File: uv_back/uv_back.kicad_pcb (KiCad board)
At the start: 2 copper layers, 75 x 174.2 mm, 0 parts

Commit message: setting up for KiCad v6.01
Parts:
- added U1: OPA1656ID, Package_SO:SOIC-8_3.9x4.9mm_P1.27mm, B.Cu at (67.6, 102.2)
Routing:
- net (no net): vias 4 -> 0
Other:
- board size 75 x 174.2 mm -> 74.8 x 173.9 mm

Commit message: dev update
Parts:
- added C1: 0.1uF, Resistor_SMD:R_0603_1608Metric, F.Cu at (99.8, 148.2)
- added C2: 0.1uF, Resistor_SMD:R_0603_1608Metric, F.Cu at (108.3, 134.2)
- added C3: 10000pF, Capacitor_SMD:C_0603_1608Metric, F.Cu at (87.4, 158.8)
- added C4: 1uF, Capacitor_SMD:C_0805_2012Metric, F.Cu at (87.6, 153.6)
- added C5: 10000pF, Capacitor_SMD:C_0603_1608Metric, F.Cu at (91.8, 153.3)
- added J1: B2B-PH-SM4-TB(LF)(SN), Connector_JST:JST_PH_B2B-PH-SM4-TB_1x02-1MP_P2.00mm_Vertical, F.Cu at (92.6, 138.2)
- added J2: B3B-PH-SM4-TB(LF)(SN), Connector_JST:JST_PH_B3B-PH-SM4-TB_1x03-1MP_P2.00mm_Vertical, F.Cu at (62.2, 120.3)
- added J3: B2B-PH-SM4-TB(LF)(SN), Connector_JST:JST_PH_B2B-PH-SM4-TB_1x02-1MP_P2.00mm_Vertical, F.Cu at (92.6, 147.8)
- added J4: B3B-PH-SM4-TB(LF)(SN), Connector_JST:JST_PH_B3B-PH-SM4-TB_1x03-1MP_P2.00mm_Vertical, F.Cu at (81.2, 138.2)
- added J5: B3B-PH-SM4-TB(LF)(SN), Connector_JST:JST_PH_B3B-PH-SM4-TB_1x03-1MP_P2.00mm_Vertical, F.Cu at (81.2, 147.8)
- added J6: B3B-PH-SM4-TB(LF)(SN), Connector_JST:JST_PH_B3B-PH-SM4-TB_1x03-1MP_P2.00mm_Vertical, F.Cu at (68.7, 157.3)
- added J7: B2B-PH-SM4-TB(LF)(SN), Connector_JST:JST_PH_B2B-PH-SM4-TB_1x02-1MP_P2.00mm_Vertical, F.Cu at (80.2, 157.3)
- added J8: B3B-PH-SM4-TB(LF)(SN), Connector_JST:JST_PH_B3B-PH-SM4-TB_1x03-1MP_P2.00mm_Vertical, F.Cu at (68.7, 147.8)
- added R1: 10k, Resistor_SMD:R_0603_1608Metric, F.Cu at (99.8, 145.7)
- added R10: 2k, Resistor_SMD:R_0603_1608Metric, F.Cu at (95.9, 153.3)
- added R11: 50, Resistor_SMD:R_0603_1608Metric, F.Cu at (103.9, 143.2)
- added R2: 10k, Resistor_SMD:R_0603_1608Metric, F.Cu at (112.3, 134.2)
- added R3: 0, Resistor_SMD:R_0603_1608Metric, F.Cu at (108.3, 136.7)
- added R4: 0, Resistor_SMD:R_0603_1608Metric, F.Cu at (87.4, 156.3)
- added R5: 1k, Resistor_SMD:R_0603_1608Metric, F.Cu at (99.8, 140.7)
- added R6: 2k, Resistor_SMD:R_0603_1608Metric, F.Cu at (91.4, 156.3)
- added R7: 1k, Resistor_SMD:R_0603_1608Metric, F.Cu at (103.9, 140.7)
- added R8: 2k, Resistor_SMD:R_0603_1608Metric, F.Cu at (108.3, 139.2)
- added R9: 2k, Resistor_SMD:R_0603_1608Metric, F.Cu at (99.8, 143.2)
- added U2: OPA1656ID, Package_SO:SOIC-8_3.9x4.9mm_P1.27mm, F.Cu at (102.1, 136.2)
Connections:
- U1 pad 1: unconnected-(U1-Pad1) -> Net-(C3-Pad2)
- U1 pad 2: unconnected-(U1-Pad2) -> Net-(C3-Pad1)
- U1 pad 3: unconnected-(U1-Pad3) -> /VMID
- U1 pad 4: unconnected-(U1-Pad4) -> GND
- U1 pad 5: unconnected-(U1-Pad5) -> Net-(J2-Pad2)
- U1 pad 6: unconnected-(U1-Pad6) -> Net-(R3-Pad1)
- U1 pad 7: unconnected-(U1-Pad7) -> Net-(R3-Pad1)
- U1 pad 8: unconnected-(U1-Pad8) -> +9V

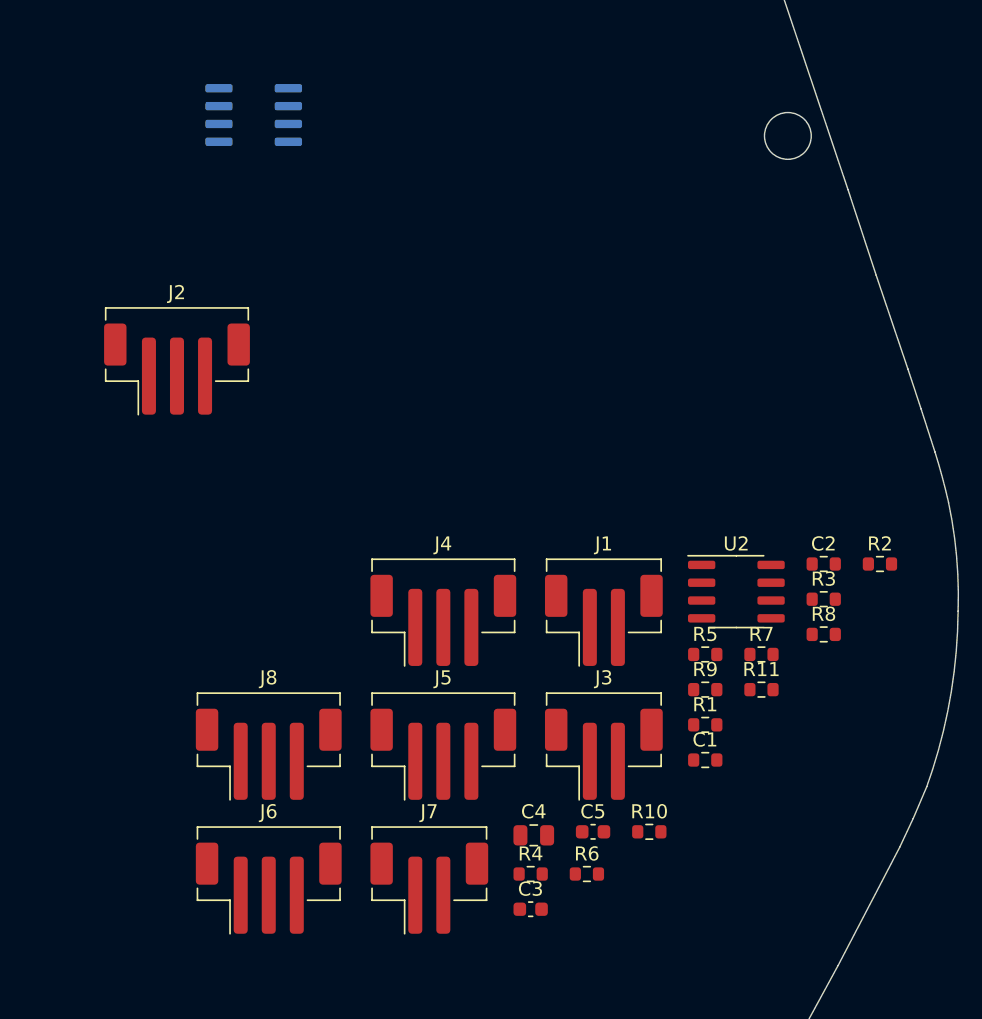
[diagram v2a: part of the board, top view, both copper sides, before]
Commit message: connector and 3d model updates
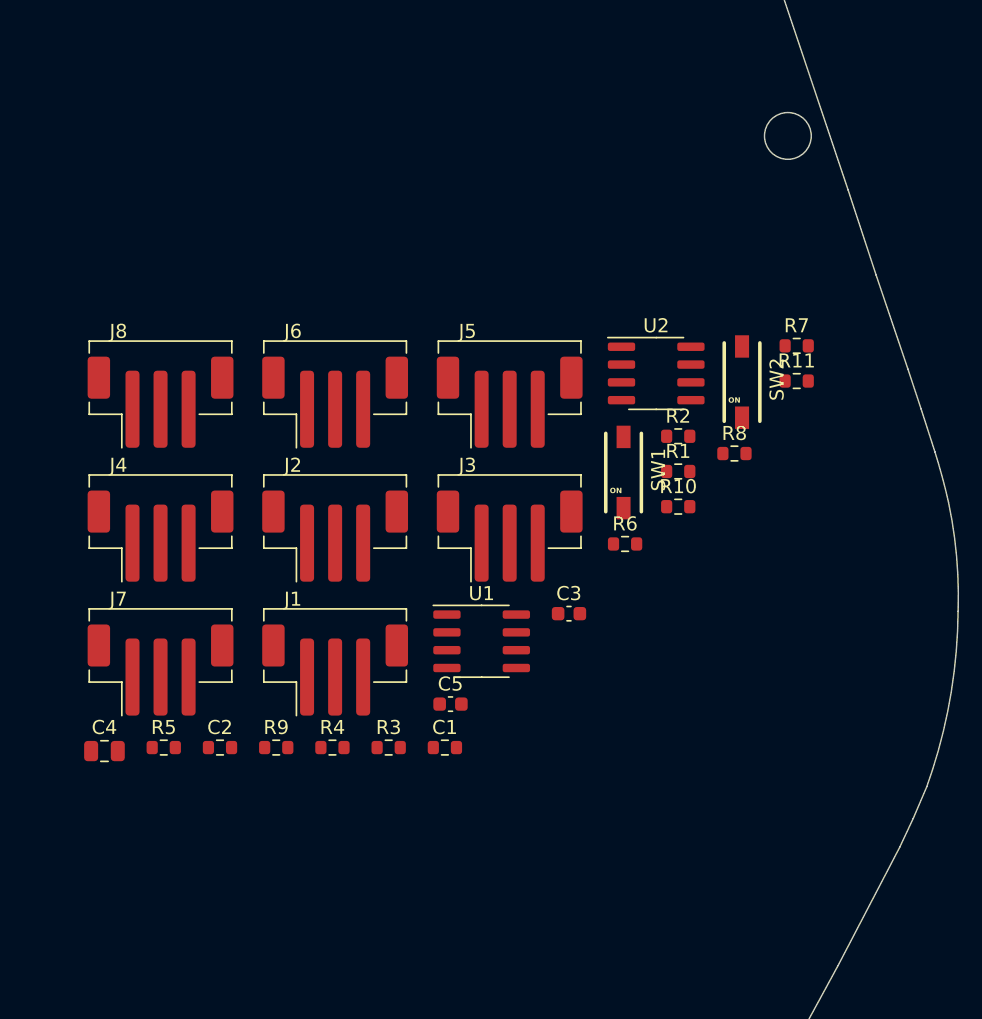
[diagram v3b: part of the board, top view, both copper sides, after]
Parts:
- added SW1: CHS01TA, eElectroMechanical:CHS-01TA, F.Cu at (94.0, 127.7)
- added SW2: CHS01TA, eElectroMechanical:CHS-01TA, F.Cu at (102.5, 121.3)
- J1, J3, J7: value B2B-PH-SM4-TB(LF)(SN) -> B3B-PH-SM4-TBT(LF)(SN); footprint Connector_JST:JST_PH_B2B-PH-SM4-TB_1x02-1MP_P2.00mm_Vertical -> eConnector_JST_PSH:B3B-PH-SM4
- J2, J4, J8: value B3B-PH-SM4-TB(LF)(SN) -> B3B-PH-SM4-TBT(LF)(SN); footprint Connector_JST:JST_PH_B3B-PH-SM4-TB_1x03-1MP_P2.00mm_Vertical -> eConnector_JST_PSH:B3B-PH-SM4
- J5, J6: value B3B-PH-SM4-TB(LF)(SN) -> B3B-PH-SM4-TBT(LF)(SN)_ALT; footprint Connector_JST:JST_PH_B3B-PH-SM4-TB_1x03-1MP_P2.00mm_Vertical -> eConnector_JST_PSH:B3B-PH-SM4
- U1: moved to F.Cu
- moved C2 45.0 mm to (65.2, 147.3)
- moved U1 40.9 mm to (83.9, 139.7), turned to 0 degrees
- moved R5 39.2 mm to (61.2, 147.3)
- moved J6 36.7 mm to (73.5, 120.9)
- moved R3 32.8 mm to (77.3, 147.3)
- moved C4 31.2 mm to (57.0, 147.6)
- moved R9 30.9 mm to (69.2, 147.3)
- moved J8 27.9 mm to (61.0, 120.9)
- moved J5 27.3 mm to (85.9, 120.9)
- moved J7 25.8 mm to (61.0, 140.0)
- moved R6 23.7 mm to (94.1, 132.8)
- moved R10 23.3 mm to (97.9, 130.1)
- moved R7 22.2 mm to (106.4, 118.7)
- moved R11 22.2 mm to (106.4, 121.2)
- moved J4 21.6 mm to (61.0, 130.5)
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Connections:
- J2 pad 1: Net-(J1-Pad1) -> Net-(J2-Pad1)
- J2 pad 2: Net-(J2-Pad2) -> GND
- J2 pad 3: /VMID -> Net-(SW2-Pad1)
- J3 pad 1: Net-(J3-Pad1) -> Net-(J2-Pad1)
- J3 pad 2: GND -> Net-(U1-Pad5)
- J4 pad 1: Net-(J3-Pad1) -> Net-(J1-Pad1)
- U1 pad 5: Net-(J2-Pad2) -> Net-(U1-Pad5)

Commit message: dev update
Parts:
- added REF**: BB-04, eBattery:BB-04, F.Cu at (74.2, 147.8)
- moved C3 93.4 mm to (139.4, 58.4)
- moved J2 93.4 mm to (122.7, 51.1)
- moved J4 93.4 mm to (110.2, 51.1)
- moved R6 93.4 mm to (143.4, 53.4)
- moved C1 93.4 mm to (130.5, 67.9)
- moved C2 93.4 mm to (114.5, 67.9)
- moved C4 93.4 mm to (106.2, 68.2)
- moved C5 93.4 mm to (130.9, 64.8)
- moved J1 93.4 mm to (122.7, 60.6)
- moved J3 93.4 mm to (135.1, 51.1)
- moved J5 93.4 mm to (135.1, 41.5)
- moved J6 93.4 mm to (122.7, 41.5)
- moved J7 93.4 mm to (110.2, 60.6)
- moved J8 93.4 mm to (110.2, 41.5)
- moved R1 93.4 mm to (147.2, 48.2)
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
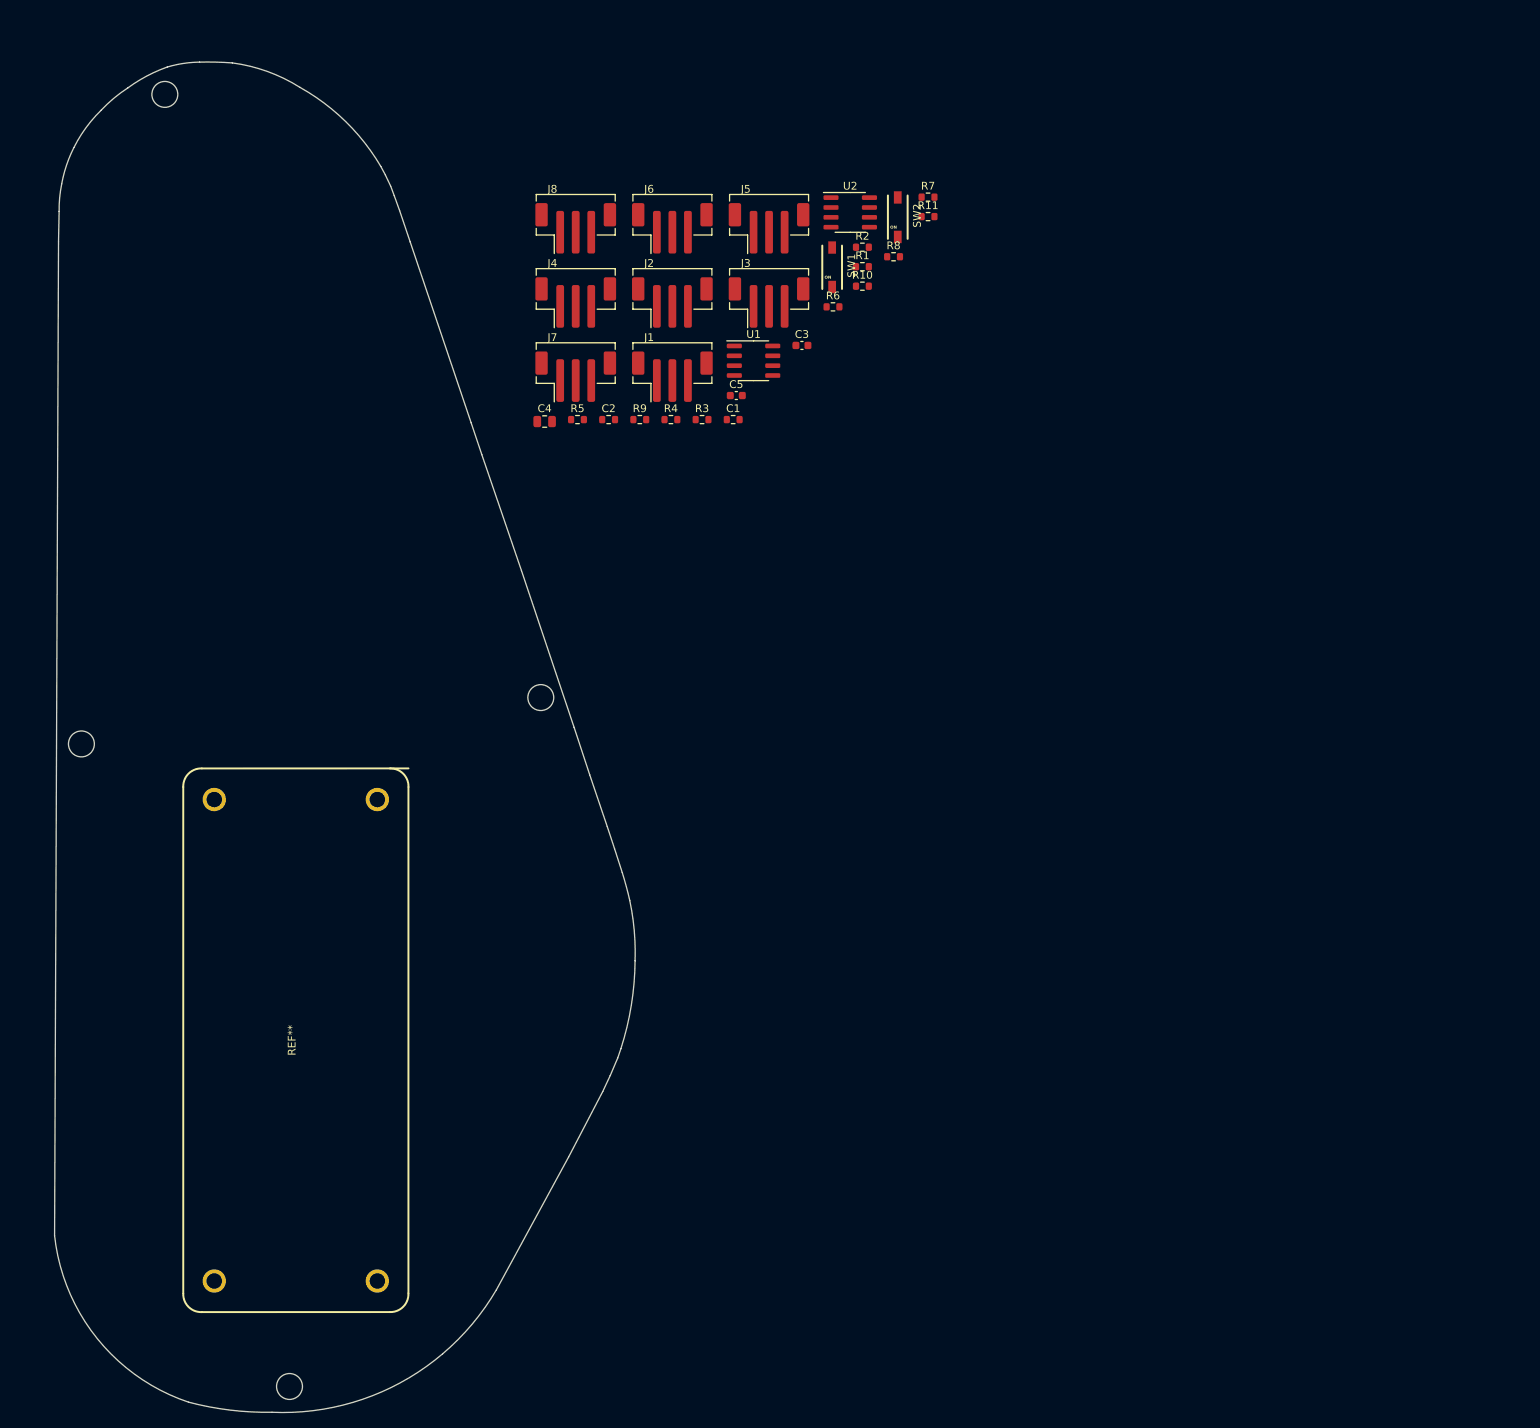
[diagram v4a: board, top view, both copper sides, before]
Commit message: 1st cut placement
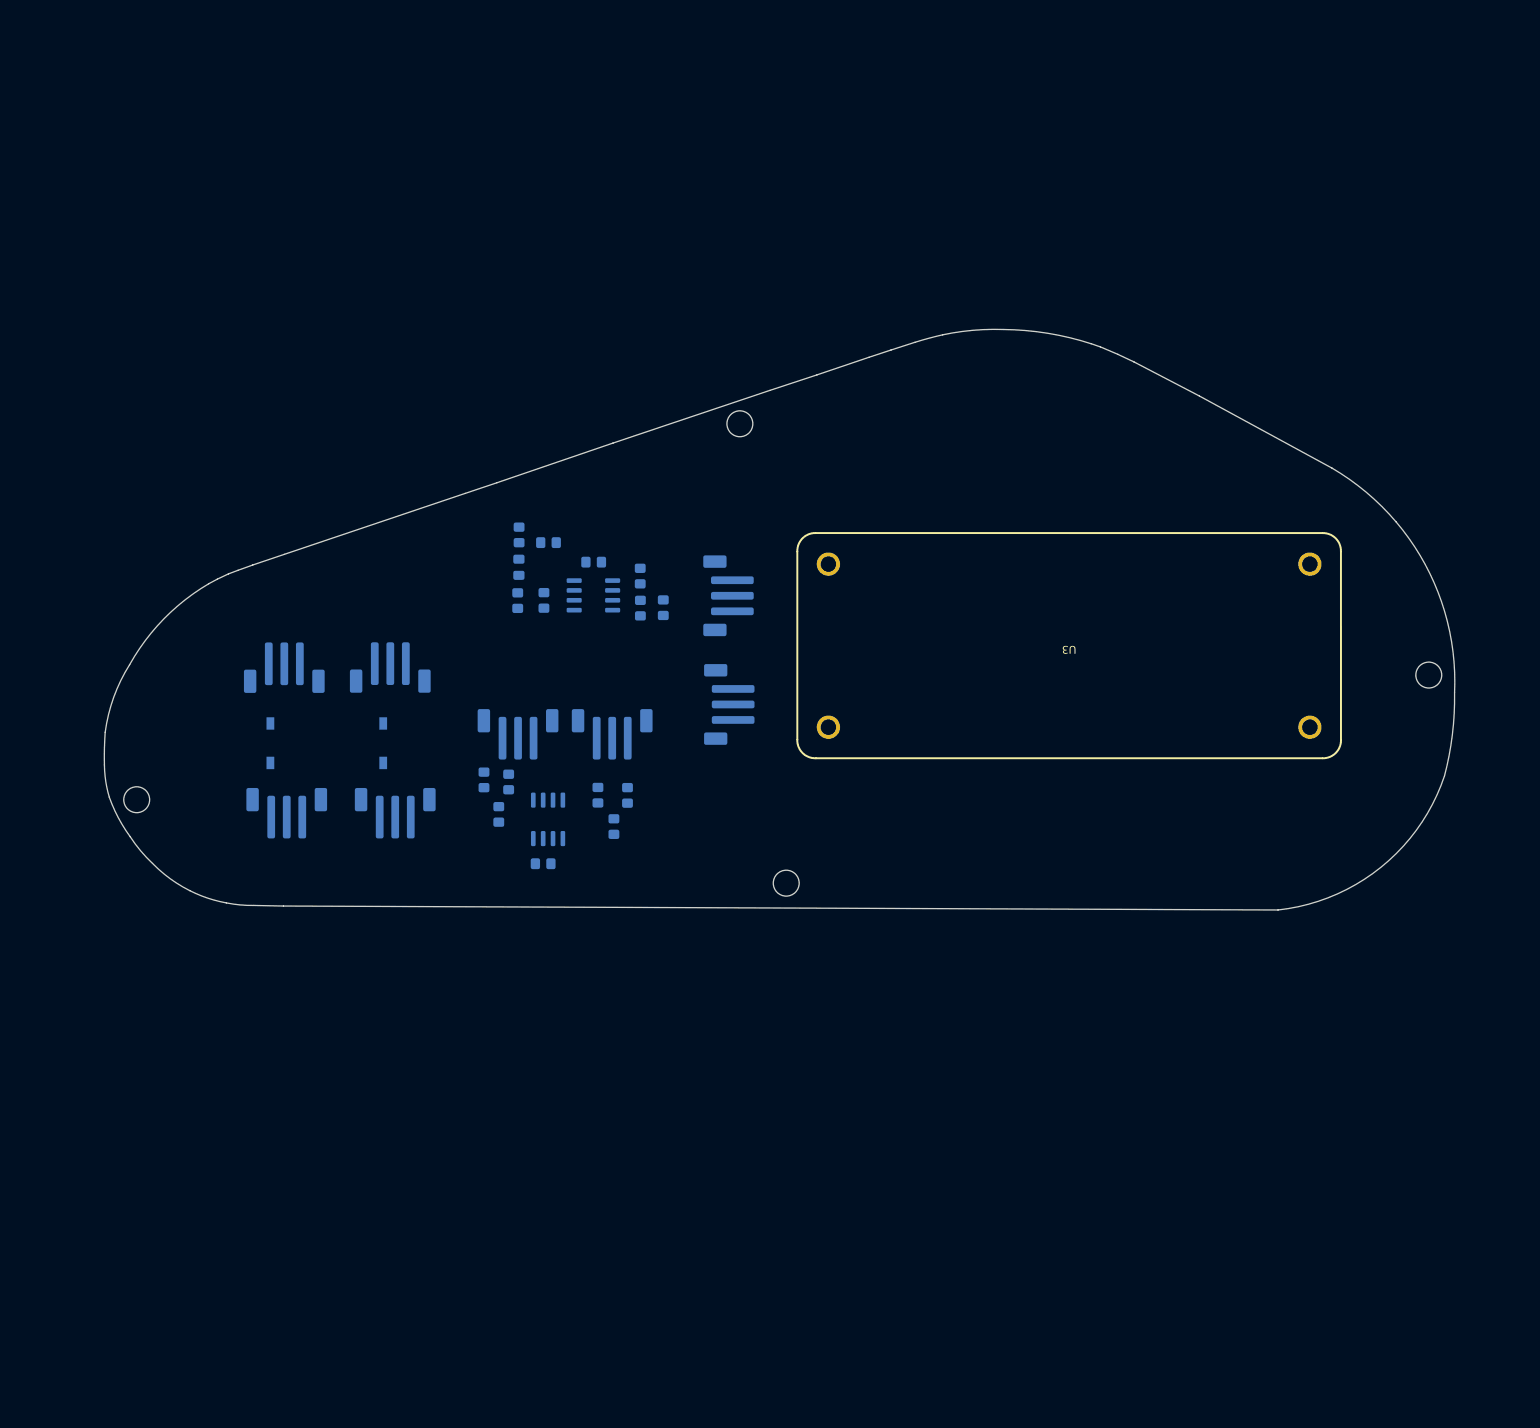
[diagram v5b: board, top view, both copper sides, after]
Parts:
- removed REF**: BB-04, eBattery:BB-04
- added U3: BB-02, eBattery:BB-04, F.Cu at (173.8, 97.0)
- C1, C2, R1, R10, R11, R2, R3, R4, R5, R6, R7, R8, R9: footprint Resistor_SMD:R_0603_1608Metric -> Resistor_SMD:R_0805_2012Metric_Pad1.20x1.40mm_HandSolder; moved to B.Cu
- C3, C5: footprint Capacitor_SMD:C_0603_1608Metric -> Resistor_SMD:R_0805_2012Metric_Pad1.20x1.40mm_HandSolder; moved to B.Cu
- C4: footprint Capacitor_SMD:C_0805_2012Metric -> Capacitor_SMD:C_0805_2012Metric_Pad1.18x1.45mm_HandSolder; moved to B.Cu
- J1, J2, J3, J4, J5, J6, J7, J8, SW1, SW2, U1, U2: moved to B.Cu
- moved SW1 94.8 mm to (70.9, 109.6), turned to 180 degrees
- moved SW2 94.8 mm to (85.4, 109.6), turned to 180 degrees
- moved R7 86.2 mm to (116.9, 116.3), turned to 90 degrees
- moved R8 79.1 mm to (113.1, 116.3), turned to 90 degrees
- moved R6 75.7 mm to (98.4, 114.3), turned to 90 degrees
- moved J1 75.0 mm to (73.0, 116.8), turned to 180 degrees
- moved J2 74.8 mm to (87.0, 116.8), turned to 180 degrees
- moved J5 72.7 mm to (102.8, 106.7), turned to 180 degrees
- moved J3 70.2 mm to (86.4, 101.6)
- moved J6 65.6 mm to (114.9, 106.7), turned to 180 degrees
- moved U1 64.7 mm to (106.7, 119.4), turned to -90 degrees
- moved R11 64.4 mm to (106.7, 83.7)
- moved J4 62.9 mm to (72.7, 101.6)
- moved C1 62.2 mm to (106.0, 125.1), turned to 180 degrees
- moved U2 59.4 mm to (112.5, 90.5), turned to 180 degrees
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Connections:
- J3 pad 2: Net-(U1-Pad5) -> Net-(J3-Pad2)
- J4 pad 2: Net-(U2-Pad5) -> Net-(J4-Pad2)
- U1 pad 1: Net-(C3-Pad2) -> Net-(R3-Pad1)
- U1 pad 2: Net-(C3-Pad1) -> Net-(R3-Pad1)
- U1 pad 3: /VMID -> Net-(J3-Pad2)
- U1 pad 5: Net-(U1-Pad5) -> Net-(J4-Pad2)
- U1 pad 6: Net-(R3-Pad1) -> Net-(R4-Pad1)
- U1 pad 7: Net-(R3-Pad1) -> Net-(R4-Pad1)
- U2 pad 5: Net-(U2-Pad5) -> /VMID
- U2 pad 6: Net-(R4-Pad1) -> Net-(C3-Pad1)
- U2 pad 7: Net-(R4-Pad1) -> Net-(C3-Pad2)
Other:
- board size 74.8 x 173.9 mm -> 173.9 x 74.8 mm
- board text added: "BRIDGE"
- board text added: "NECK"
- board text added: "PICKUP"
- board text added: "POT"
- board text added: "SWITCH"
